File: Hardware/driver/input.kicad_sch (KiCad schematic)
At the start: 24 parts, among them J301 TBP01R2W-508-02BE, Q301 IXTH80N075L2, Q302 IXTH80N075L2, U301 MCP3426-xMS, U302 ADS1000A1, U303 DAC60501, U304 DAC60501, U305 DS18B20, U306 DS18B20

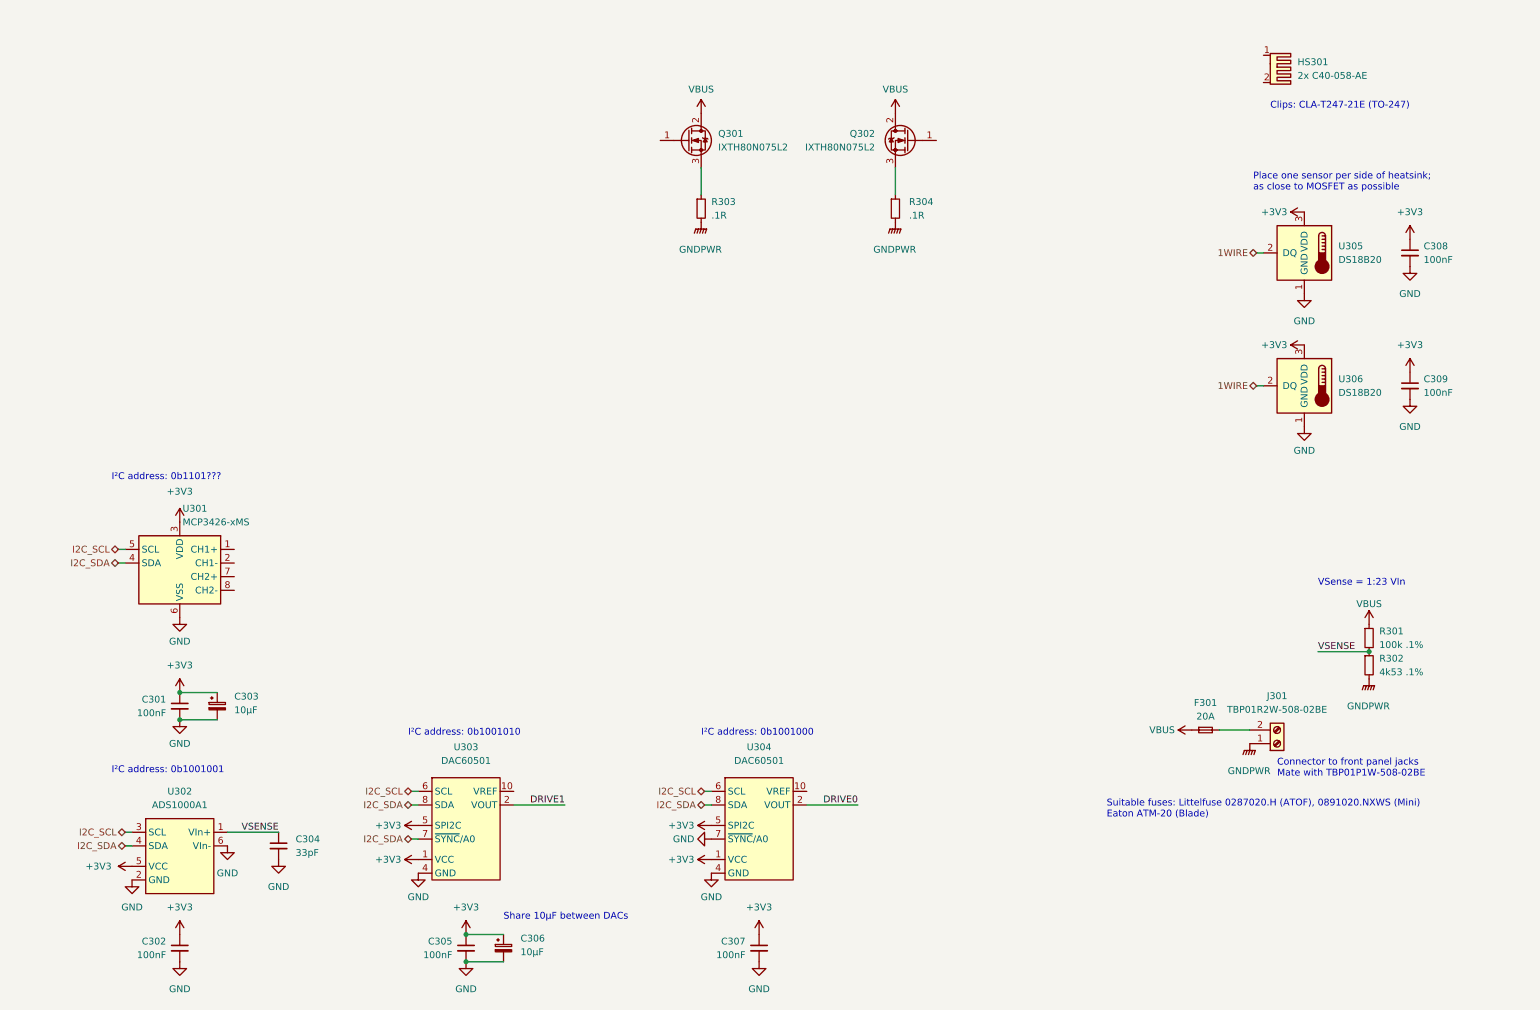
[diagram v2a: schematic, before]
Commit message: More work on PCB; load control drivers
- Added in the schematic part of the opamp based gate drivers, and the
  current sense stuff. Changed out the double ADC for a pair of single
  ADCs, and also use the same ADC for everything to reduce required line
  items on BOM

- Routed a chunk of the power section and fan controller of the board

- Added mains AC/DC converter brick, it can be bypassed with an external
  +12V input instead, if desired
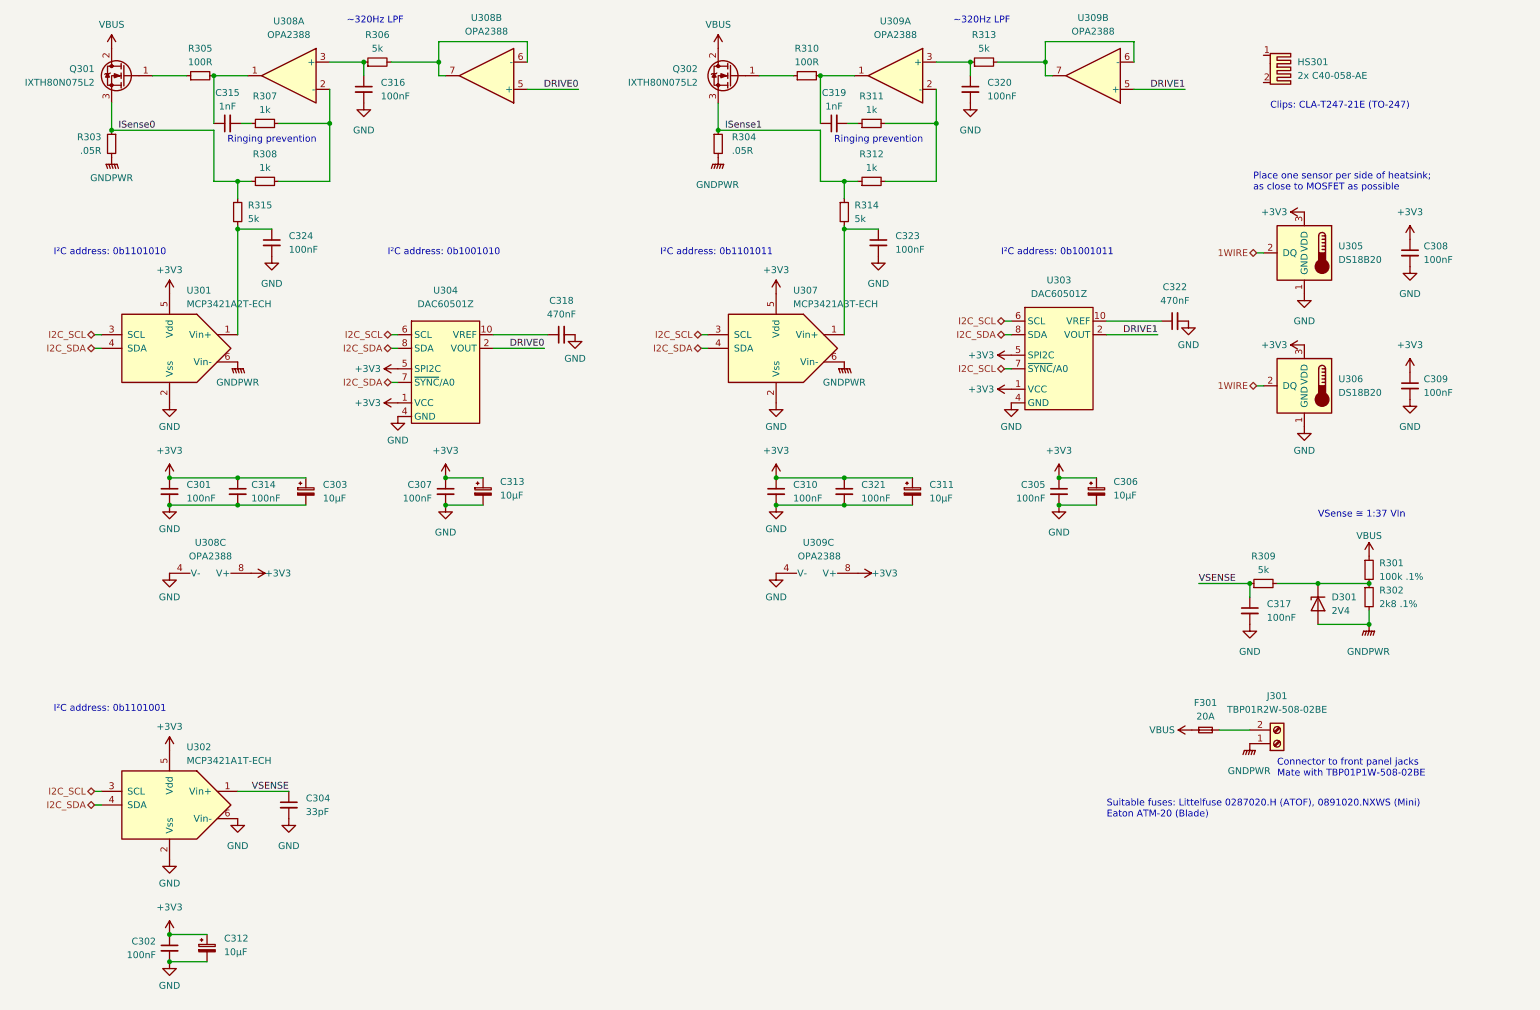
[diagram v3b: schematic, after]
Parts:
- removed U301: MCP3426-xMS, Package_SO:MSOP-8_3x3mm_P0.65mm, symbol Analog_ADC:MCP3426-xMS
- removed U302: ADS1000A1, Package_TO_SOT_SMD:SOT-23-6_Handsoldering, symbol programmable-load:ADS1000A1
- added C310, C314, C316, C317, C320, C321, C323, C324: 100nF, Capacitor_SMD:C_0805_2012Metric_Pad1.18x1.45mm_HandSolder, symbol Device:C_Small
- added C311, C312, C313: 10µF, Capacitor_Tantalum_SMD:CP_EIA-3216-18_Kemet-A_Pad1.58x1.35mm_HandSolder, symbol Device:C_Polarized_Small
- added C315, C319: 1nF, Capacitor_SMD:C_0805_2012Metric_Pad1.18x1.45mm_HandSolder, symbol Device:C_Small
- added C318, C322: 470nF, Capacitor_SMD:C_0805_2012Metric_Pad1.18x1.45mm_HandSolder, symbol Device:C_Small
- added D301: 2V4, Diode_SMD:D_MiniMELF_Handsoldering, symbol Device:D_Zener
- added R305, R310: 100R, Resistor_SMD:R_0805_2012Metric_Pad1.20x1.40mm_HandSolder, symbol Device:R_Small
- added R306, R309, R313, R314, R315: 5k, Resistor_SMD:R_0805_2012Metric_Pad1.20x1.40mm_HandSolder, symbol Device:R_Small
- added R307, R308, R311, R312: 1k, Resistor_SMD:R_0805_2012Metric_Pad1.20x1.40mm_HandSolder, symbol Device:R_Small
- added U301: MCP3421A2T-ECH, Package_TO_SOT_SMD:SOT-23-6_Handsoldering, symbol Analog_ADC:MCP3421A0T-ECH
- added U302: MCP3421A1T-ECH, Package_TO_SOT_SMD:SOT-23-6_Handsoldering, symbol Analog_ADC:MCP3421A0T-ECH
- added U307: MCP3421A3T-ECH, Package_TO_SOT_SMD:SOT-23-6_Handsoldering, symbol Analog_ADC:MCP3421A0T-ECH
- added U308, U309: OPA2388, Package_SO:SOIC-8_3.9x4.9mm_P1.27mm, symbol programmable-load:OPA2388
- C303, C306: footprint (none) -> Capacitor_Tantalum_SMD:CP_EIA-3216-18_Kemet-A_Pad1.58x1.35mm_HandSolder; MPN (none) -> TAJA106K016RNJ
- R302: value 4k53 .1% -> 2k8 .1%; MPN ERA-8AEB4531V -> TNPW12062K80BEEA
- R303, R304: value .1R -> .05R
- U303, U304: value DAC60501 -> DAC60501Z
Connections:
- net +3V3: now also C310.1, C311.1, C312.1, C313.1, C314.1, C321.1, U301.5 (Vdd), U302.5 (Vdd), U307.5 (Vdd), U308.8 (V+), U309.8 (V+)
- net DRIVE0: now also U308.5 (+)
- net DRIVE1: now also U309.5 (+)
- net GND: now also C310.2, C311.2, C312.2, C313.2, C314.2, C316.2, C317.2, C318.2, C320.2, C321.2, C322.2, C323.2, C324.2, U301.2 (Vss), U302.2 (Vss), U302.6 (Vin-), U307.2 (Vss), U308.4 (V-), U309.4 (V-); no longer U304.7 (~{SYNC}/A0)
- net GNDPWR: now also D301.2 (A), U301.6 (Vin-), U307.6 (Vin-)
- net I2C_SCL: now also U303.7 (~{SYNC}/A0), U301.3 (SCL), U302.3 (SCL), U307.3 (SCL)
- net I2C_SDA: now also U304.7 (~{SYNC}/A0), U301.4 (SDA), U302.4 (SDA), U307.4 (SDA); no longer U303.7 (~{SYNC}/A0)
- net VSENSE: now also C317.1, R309.1, U302.1 (Vin+); no longer R301.2, R302.1
- net ISense1: now reaches Q302.3 (S), R304.1
- net ISense1: now also R312.1, R314.1
- net at Q301.1 (G): now also R305.1
- net ISense0: now reaches Q301.3 (S), R303.1
- net ISense0: now also R308.1, R315.1
- net at U304.10 (VREF): now also C318.1
- net at Q302.1 (G): now also R310.1
- net at U303.10 (VREF): now also C322.1
- new net: C315.1, R305.2, U308.1
- new net: R307.2, R308.2, U308.2 (-)
- new net: C316.1, R306.1, U308.3 (+)
- new net: C324.1, R315.2, U301.1 (Vin+)
- new net: C319.1, R310.2, U309.1
- new net: R311.2, R312.2, U309.2 (-)
- new net: C320.1, R313.1, U309.3 (+)
- new net: C319.2, R311.1
- new net: D301.1 (K), R301.2, R302.1, R309.2
- new net: R306.2, U308.6 (-), U308.7
- new net: R313.2, U309.6 (-), U309.7
- new net: C323.1, R314.2, U307.1 (Vin+)
- new net: C315.2, R307.1
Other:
- note added: "I²C address: 0b1001011"
- note added: "I²C address: 0b1101001"
- note added: "I²C address: 0b1101010"
- note added: "I²C address: 0b1101011"
- note added: "Ringing prevention"
- note added: "VSense ≅ 1:37 VIn"
- note added: "~320Hz LPF"
- note removed: "I²C address: 0b1001000"
- note removed: "I²C address: 0b1001001"
- note removed: "I²C address: 0b1101???"
- note removed: "Share 10µF between DACs"
- note removed: "VSense = 1:23 VIn"
- moved on the sheet: C301, C303, C304, C305, C306, C307, Q301, Q302, R301, R302, R303, R304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

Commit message: Layed out gate driver, current sense
- Placed and routed the current sense ADCs, as well as the op amps and
  DACs for controlling the gate drive, and the voltage sensing ADC. We
  just need to route a few of the high current traces, and snake the
  1Wire/I2C bus around and it should be good to go

  Also, the IO expander: it needs to be placed or just removed since
  we're not really using it for anything…
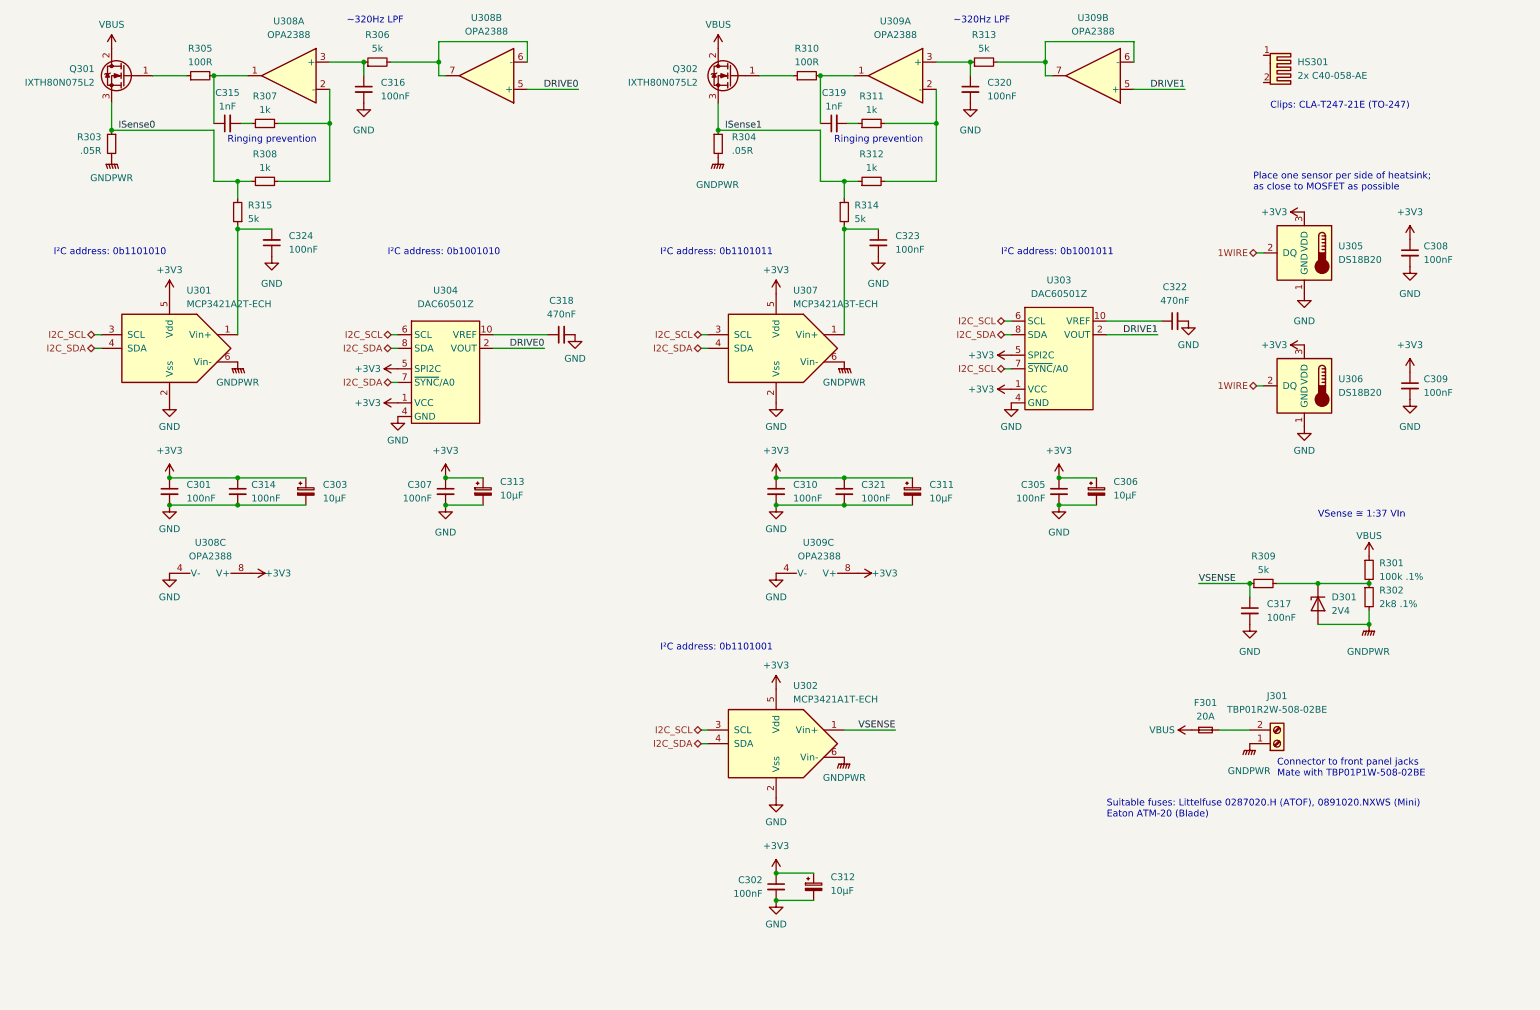
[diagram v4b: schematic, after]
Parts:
- removed C304: 33pF, Capacitor_SMD:C_0805_2012Metric_Pad1.18x1.45mm_HandSolder, symbol Device:C_Small
- R301: MPN CRT1206-BY-1003ELF -> TNPW1206100KBYEA
- R302: MPN TNPW12062K80BEEA -> ERA-8ARB2801V
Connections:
- net GND: now also C324.1; no longer C324.2, U302.6 (Vin-)
- net GNDPWR: now also U302.6 (Vin-)
- net ISense0: now also R308.2, R315.2; no longer R308.1, R315.1
- net at R307.2, U308.2 (-): now also R308.1; no longer R308.2
- new net: C324.2, R315.1, U301.1 (Vin+)
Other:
- moved on the sheet: C302, C312, C324, R308, R315, U302
